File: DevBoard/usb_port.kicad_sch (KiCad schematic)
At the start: 105 parts, among them J501 TYPE-C 16PCB0.8 IP68, J502 I2CC logic analyzer, Q501 IAUC45N04S6L063H, Q502 IAUC45N04S6L063H, U501 TPS25751DREFR, U502 M24512-DFMC6TG, U503 BQ25756RRVR, U504 TPS62933DRLR

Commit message: Dev board rev A4: design-review fixes, polymer bulk, charge inhibit
Schematic design review (three reviewers, cross-challenged) in
docs/devboard/schematic-review-2026-10-12.md, and its fixes:
- U203 TPS70950 EN no longer tied to PACK_P (would destroy it)
- ICHG 17.8k: 2.8 A per port (was 9.8 A, above the cells' 5.6 A)
- U101 footprint from TI RSM0032A (1.4 mm thermal pad, was 2.8 mm)
- D+/D- ESD now 5 V PESD5V0S2BT (TPS25751 GPIO4/5 are rated 6 V)
- R101-R104 1206, F101 and J101 DNP, DNP gate parts on Q102
- BTP_INT buffered by a 2N7002; SMBus pull-ups on a removable 0R
- Wake button, bench PACK_P header, reset, BOOT0/3V3_SLEEP pads,
  J303 series resistors, IRQ pull-ups, vertical SMAs, BOM ratings

Open-question decisions: CHG_INH (PB8 -> each BQ25756 CE) lets the
MCU stop charging independently of the TPS25751; J103 in EV2400
SMBus pin order; "fit cells before USB" silkscreen.

Charger bulk banks now one solid polymer cap plus the MLCCs at the
FETs (16 fewer MLCCs). PWR_FLAGs moved to where each rail is sourced.
Board: footprints swapped/added and placed, DRC clean before routing.

Co-Authored-By: Claude Opus 5.5 <noreply@anthropic.com>
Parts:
- removed C522, C525, C526, C528, C529: 22u 35V, Capacitor_SMD:C_1210_3225Metric, symbol Device:C
- removed C533, C536, C537: 47u 25V, Capacitor_SMD:C_1210_3225Metric, symbol Device:C
- added C547: 10p, Capacitor_SMD:C_0603_1608Metric, symbol Device:C
- added R535: 1k, Resistor_SMD:R_0603_1608Metric, symbol Device:R
- C501, C502: value 330p -> 330p 50V; LCSC (none) -> C13533; MPN (none) -> CL05C331JB5NNNC
- C508: value 0.1u -> 0.1u 50V; LCSC (none) -> C307331; MPN (none) -> CL05B104KB54PNC
- C509: value 1u 35V (VAC) -> 1u 50V (VAC); footprint Capacitor_SMD:C_0603_1608Metric -> Capacitor_SMD:C_0805_2012Metric; LCSC (none) -> C28323; MPN (none) -> CL21B105KBFNNNE; Notes (none) -> VAC cap: 50 V 0805 keeps ~1 uF at 20 V (review m20)
- C521: value 22u 35V -> 68u 35V; footprint Capacitor_SMD:C_1210_3225Metric -> Capacitor_SMD:CP_Elec_6.3x5.8; symbol Device:C -> Device:C_Polarized; LCSC C778721 -> C49435121; MPN GMK325BJ226MM-P -> ChuangHui SV680M350E5R8R4Z00ZZ (polymer); Notes (none) -> USB-side bulk: solid polymer, no DC-bias loss (68 uF at 20 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
- C532: value 47u 25V -> 100u 25V; footprint Capacitor_SMD:C_1210_3225Metric -> Capacitor_SMD:CP_Elec_6.3x5.8; symbol Device:C -> Device:C_Polarized; LCSC C90142 -> C46550465; MPN TMK325ABJ476MM-P -> JIERR MA25V100M6x6 (polymer); Notes (none) -> Battery-side bulk: solid polymer, no DC-bias loss (100 uF a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
- D503: value ESD2CAN24DBZRQ1 -> PESD5V0S2BT; LCSC C5736151 -> C49338; MPN (none) -> PESD5V0S2BT,215; Notes (none) -> D+/D- go to TPS25751 GPIO4/5 (6 V abs max): 5 V working, 5.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
- R513: value 5.11k 0.1% -> 17.8k 0.1%; LCSC C705788 -> C705729; MPN (none) -> RT0603BRD0717K8L; Notes ICHG 9.8 A -> ICHG hardware ceiling 50/17.8 = 2.8 A per port (5.6 A both 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
- R531: footprint Resistor_SMD:R_1206_3216Metric -> Resistor_SMD:R_2512_6332Metric; LCSC (none) -> C2907567; MPN (none) -> FRC2512P000TS; Notes PACK_P link -> 2512 0R: carries up to ~1.7 A TPS62933 input (review m19)
- R533: value 105k 0.1% -> 107k 0.1%; LCSC C865128 -> C865130; MPN (none) -> RT0805BRD07107KL; Notes (none) -> PP5V = 0.8 x (1 + 107/20) = 5.08 V: margin over the TPS2575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
- TH501: LCSC (none) -> C13564; MPN (none) -> NCP18XH103F03RB
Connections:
- net CE_N: now also R535.2
- net PP5V: now also C547.1
- net at R533.2, R534.1, U504.8 (FB): now also C547.2
- new net CHG_INH: R535.1
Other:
- note added: "BATTERY-SIDE BULK: 3 x 47u MLCC + 100u polymer (>= 80 uF effective)"
- note added: "BQ25756 CONTROLLER (600 kHz, ICHG 2.8 A, ILIM 5.5 A, VAC 4.1-22.5 V window)"
- note added: "NOTES (this sheet is used twice: USB Port 1 = 4xx, USB Port 2 = 5xx) 1. Address straps are on the root sheet: port 1 ADCIN1 = LDO_3V3, ADCIN2 = GND (0x20); port 2 ADCIN1 = ADCIN2 = GND (0x21). R405-R408 are DNP divider footprints for other options. 2. Unused TPS25751 GPIOs tied to GND per datasheet (KiCad ERC flags this; expected). 3. At the connector pins: D402 CC ESD (24 V), D403 D+/D- ESD (5 V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"
- note added: "USB-SIDE BULK: 4 x 22u MLCC + 68u polymer (>= 80 uF effective)"
- note removed: "BATTERY-SIDE BULK (>= 80 uF effective after DC bias)"
- note removed: "BQ25756 CONTROLLER (600 kHz, ICHG 9.8 A, ILIM 5.5 A, VAC 4.1-22.5 V window)"
- note removed: "NOTES (this sheet is used twice: USB Port 1 = 4xx, USB Port 2 = 5xx) 1. Address straps are on the root sheet: port 1 ADCIN1 = LDO_3V3, ADCIN2 = GND (0x20); port 2 ADCIN1 = ADCIN2 = GND (0x21). R405-R408 are DNP divider footprints for other options. 2. Unused TPS25751 GPIOs tied to GND per datasheet (KiCad ERC flags this; expected). 3. D402/D403 (24 V rated ESD) and C401/C402 right at the connecto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"
- note removed: "USB-SIDE BULK (>= 80 uF effective after DC bias)"
- moved on the sheet: C523, C524, C527, C530, C531, C534, C535

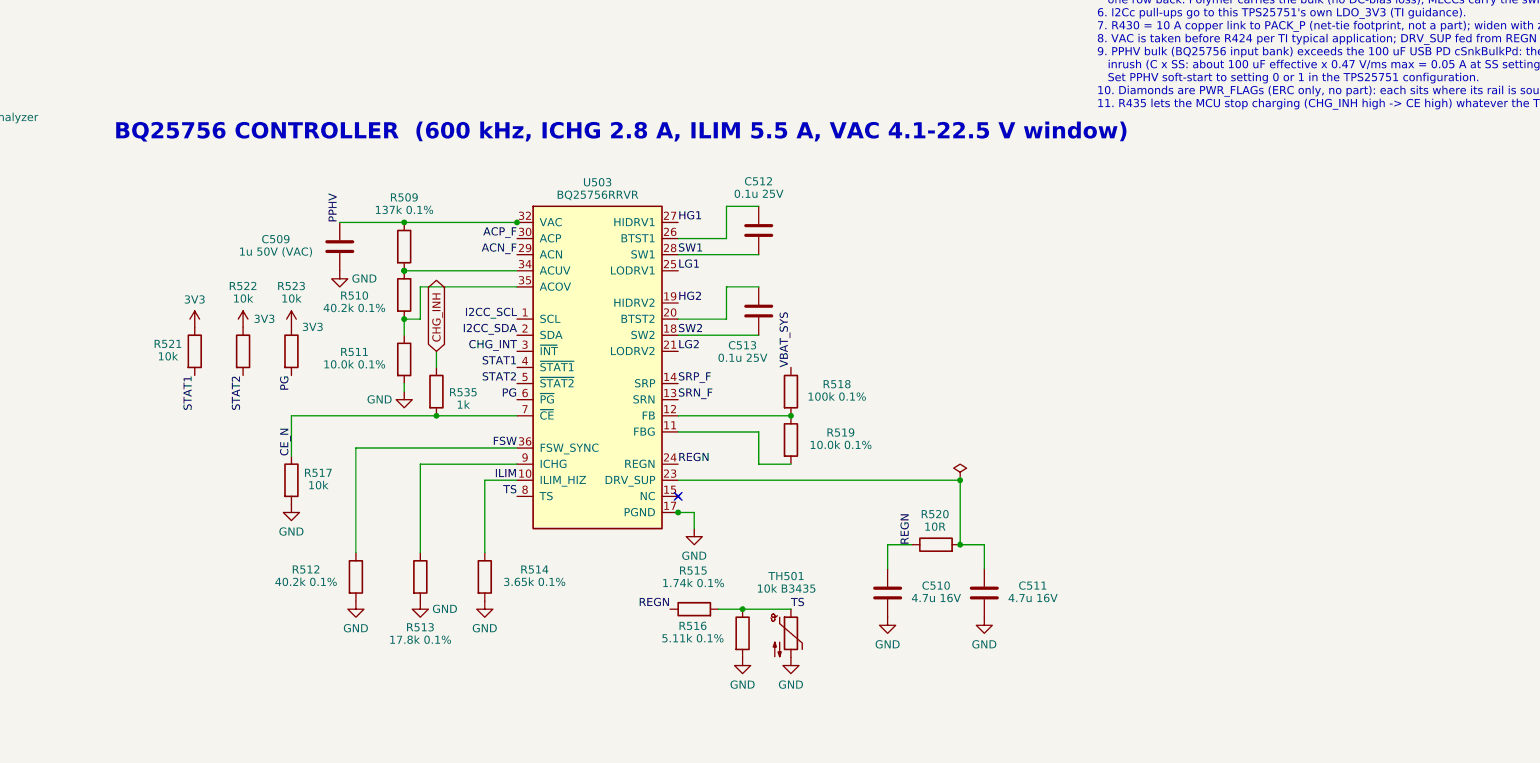
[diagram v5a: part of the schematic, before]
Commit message: Dev board: ICHG ceiling 5.5 A per port so one port can charge at 1C
R413/R513 17.8k -> 9.09k (5.3-5.7 A hardware ceiling per port).
Both-port total stays at 5.6 A through configuration and firmware:
TPS25751 starts each charger at ICHG_REG 2.8 A, the MCU raises the
only charging port and drops it again on the other port's attach
interrupt; watchdog expiry stops charging (EN_CHG_BIT_RESET_BEHAVIOR
= 0). Documented as firmware item 14 in the review.

Co-Authored-By: Claude Opus 5.5 <noreply@anthropic.com>
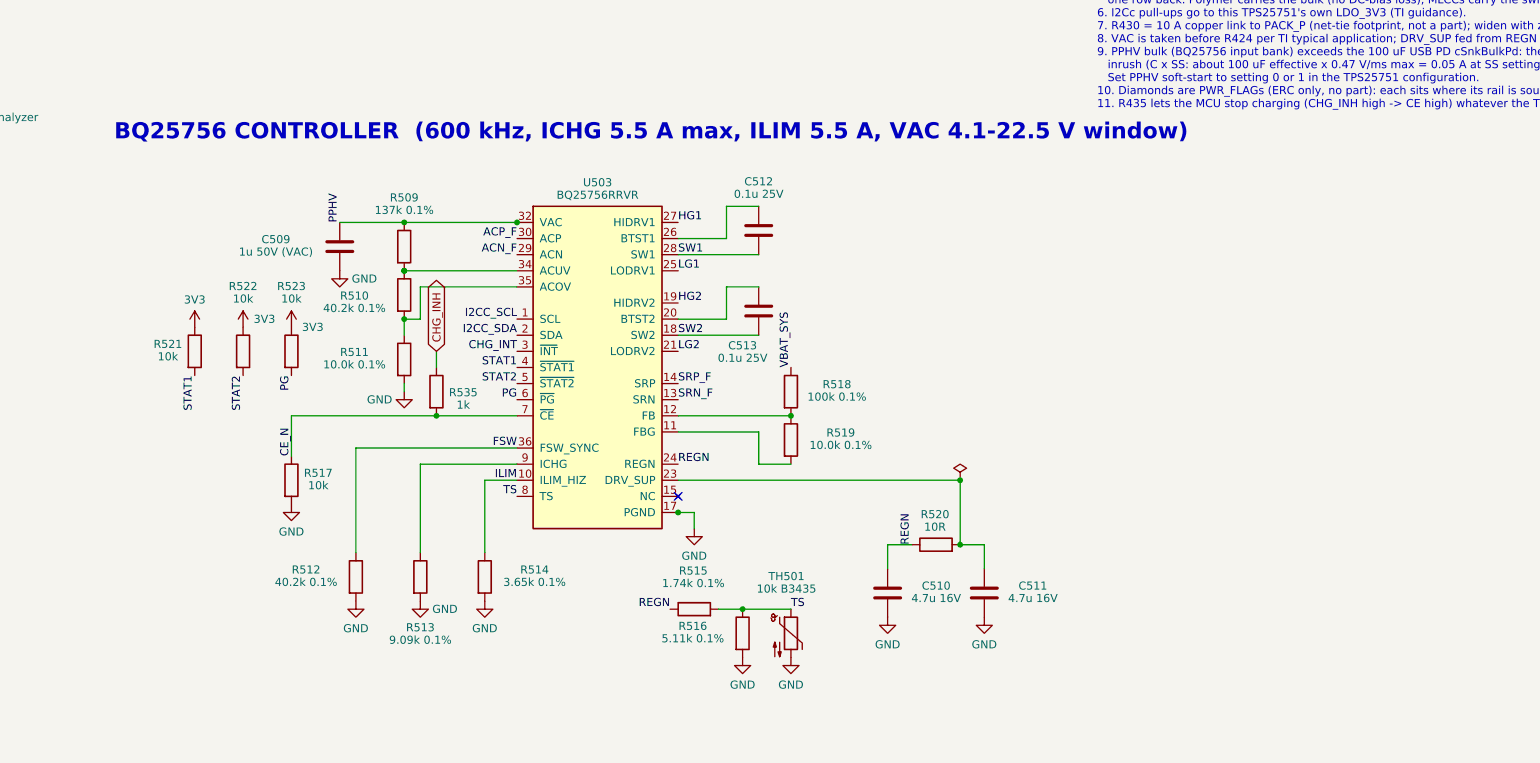
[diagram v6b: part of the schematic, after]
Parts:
- R513: value 17.8k 0.1% -> 9.09k 0.1%; LCSC C705729 -> (none); MPN RT0603BRD0717K8L -> RT0603BRD079K09L; Notes ICHG hardware ceiling 50/17.8 = 2.8 A per port (5.6 A both 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 -> ICHG hardware ceiling 50/9.09 = 5.5 A per port (5.3-5.7 A):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
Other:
- note added: "BQ25756 CONTROLLER (600 kHz, ICHG 5.5 A max, ILIM 5.5 A, VAC 4.1-22.5 V window)"
- note removed: "BQ25756 CONTROLLER (600 kHz, ICHG 2.8 A, ILIM 5.5 A, VAC 4.1-22.5 V window)"
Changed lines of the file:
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@@
 		)
 	)
-	(text "BQ25756 CONTROLLER  (600 kHz, ICHG 2.8 A, ILIM 5.5 A, VAC 4.1-22.5 V window)"
+	(text "BQ25756 CONTROLLER  (600 kHz, ICHG 5.5 A max, ILIM 5.5 A, VAC 4.1-22.5 V window)"
 		(exclude_from_sim no)
 		(at 304.8 167.64 0)
@@
 			)
 		)
-		(property "Value" "17.8k 0.1%"
+		(property "Value" "9.09k 0.1%"
 			(at 353.06 246.17 0)
 			(show_name no)
@@
 			)
 		)
-		(property "Notes" "ICHG hardware ceiling 50/17.8 = 2.8 A per port (5.6 A both ports = cell 1C); charger falls back to it on watchdog expiry (review #2)"
+		(property "Notes" "ICHG hardware ceiling 50/9.09 = 5.5 A per port (5.3-5.7 A): one port can charge at about 1C. Firmware keeps the sum of both ports at 5.6 A max (TPS25751 config default ICHG_REG 2.8 A; MCU raises the only charging port). EN_CHG_BIT_RESET_BEHAVIOR = 0 so a watchdog expiry stops charging instead of falling back to this pin"
 			(at 2.54 0 0)
 			(hide yes)
@@
 			)
 		)
-		(property "LCSC" "C705729"
+		(property "LCSC" ""
 			(at 353.06 236.22 0)
 			(hide yes)
@@
 			)
 		)
-		(property "MPN" "RT0603BRD0717K8L"
+		(property "MPN" "RT0603BRD079K09L"
 			(at 353.06 236.22 0)
 			(hide yes)

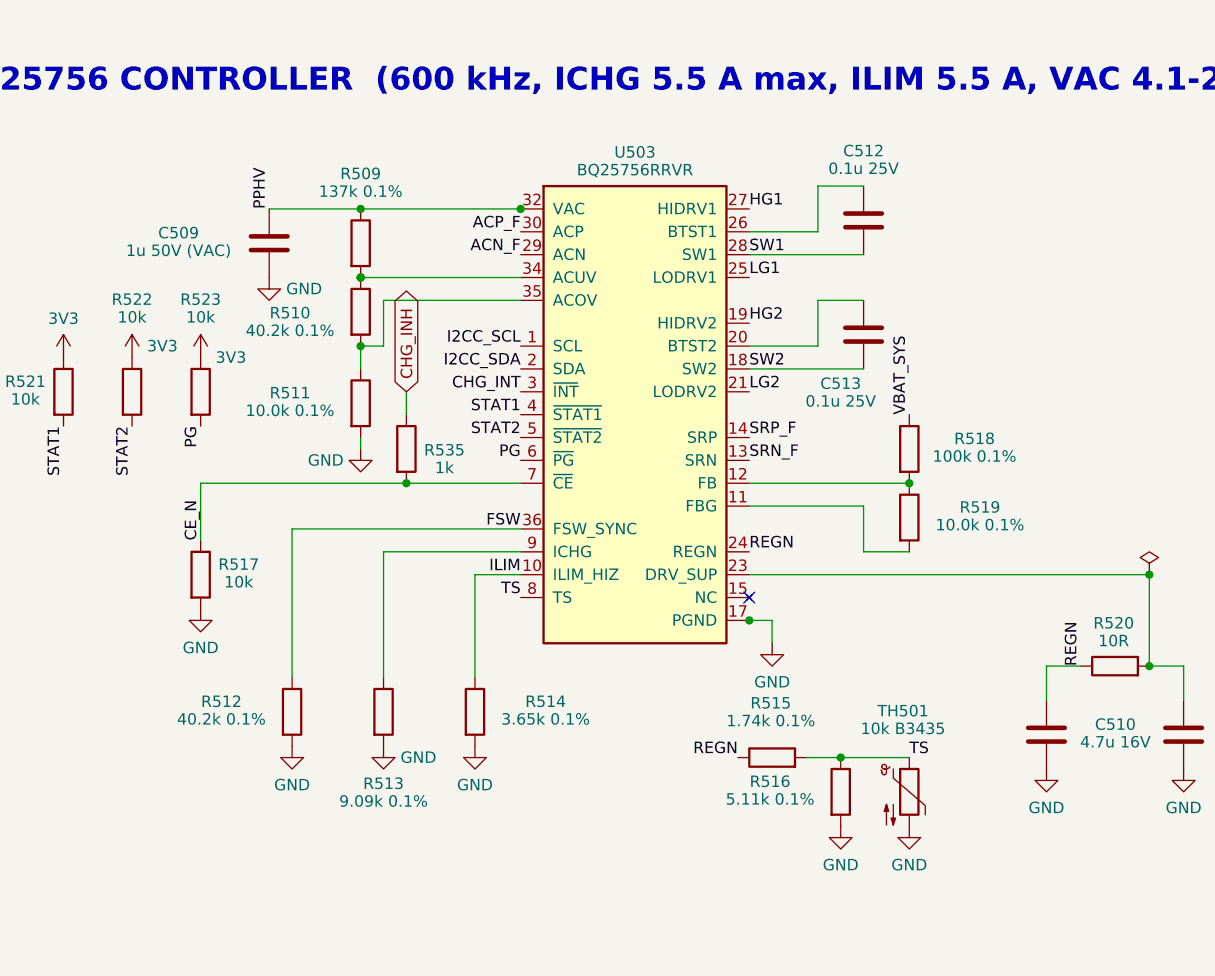
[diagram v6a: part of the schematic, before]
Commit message: Dev board: bootstrap diodes, one NTC per cell, 1 % resistors
- BQ25756 bootstrap Schottkys DRV_SUP -> BTST1/BTST2 on both ports
  (TI BQ25756 schematic checklist D2/D3, required; LRB521S-40T1G,
  SOD-523), placed in line with the BTST caps. Also added to the
  production BOM/netlist.
- Gauge TS2-TS4 no longer tied to VSS: J105-J107 take a wired 10k NTC
  per cell; all four NTC headers sit beside their cell's tap test point.
- Precision resistors rounded to stocked UNI-ROYAL 1 % parts (ICHG
  9.1k, ILIM 3.6k, TS 1.8k/5.6k, FSW/ACUV-ACOV, NTC dividers); only the
  charge-voltage and PP5V feedback dividers stay 0.1 %.

Co-Authored-By: Claude Opus 5.5 <noreply@anthropic.com>
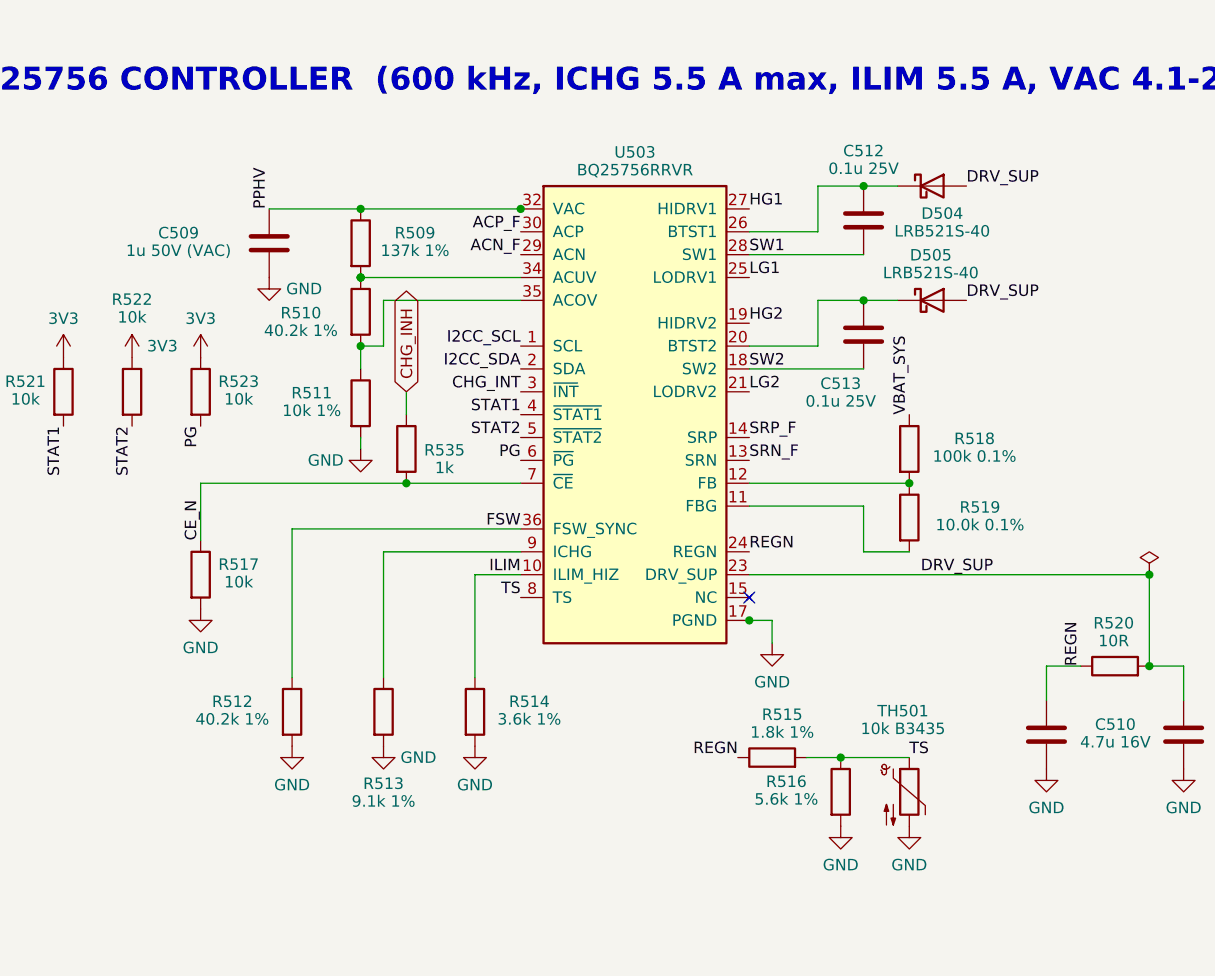
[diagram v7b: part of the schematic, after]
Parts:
- added D504, D505: LRB521S-40, Diode_SMD:D_SOD-523, symbol Device:D_Schottky
- R509: value 137k 0.1% -> 137k 1%; footprint Resistor_SMD:R_0805_2012Metric -> Resistor_SMD:R_0603_1608Metric; LCSC (none) -> C22872; MPN (none) -> 0603WAF1373T5E; Notes RAC1 -> ACUV/ACOV divider top: OV stop 1.2 x 187.2/10 = 22.5 V, UV 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
- R510: value 40.2k 0.1% -> 40.2k 1%; LCSC C865475 -> C17678; MPN (none) -> 0805W8F4022T5E; Notes RAC2 -> ACUV/ACOV divider middle
- R511: value 10.0k 0.1% -> 10k 1%; LCSC C110775 -> C17414; MPN (none) -> 0805W8F1002T5E; Notes RAC3 -> ACUV/ACOV divider bottom
- R512: value 40.2k 0.1% -> 40.2k 1%; LCSC C865475 -> C17678; MPN (none) -> 0805W8F4022T5E; Notes 600 kHz -> FSW ~600 kHz; the oscillator is +/-15 %, so 1 % is plenty
- R513: value 9.09k 0.1% -> 9.1k 1%; LCSC (none) -> C23260; MPN RT0603BRD079K09L -> 0603WAF9101T5E; Notes ICHG hardware ceiling 50/9.09 = 5.5 A per port (5.3-5.7 A):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 -> ICHG hardware ceiling 50/9.1 = 5.5 A per port (5.3-5.8 A ov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
- R514: value 3.65k 0.1% -> 3.6k 1%; LCSC C705773 -> C22980; MPN (none) -> 0603WAF3601T5E; Notes ILIM 5.5 A -> ILIM_HIZ hardware input ceiling 50 x 2/5 / 3.6 = 5.6 A (5.3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
- R515: value 1.74k 0.1% -> 1.8k 1%; LCSC C784581 -> C4177; MPN (none) -> 0603WAF1801T5E; Notes RT1 -> TS RT1 (REGN to TS). With R416 5.6k and the 10k B3435 FET N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
- R516: value 5.11k 0.1% -> 5.6k 1%; LCSC C705788 -> C23189; MPN (none) -> 0603WAF5601T5E; Notes RT2 -> TS RT2 (TS to GND), see R415
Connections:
- net at C513.1, U503.20 (BTST2): now also D505.1 (K)
- net DRV_SUP: now reaches C511.1, R520.2, U503.23 (DRV_SUP)
- net DRV_SUP: now also D504.2 (A), D505.2 (A)
- net at C512.1, U503.26 (BTST1): now also D504.1 (K)
